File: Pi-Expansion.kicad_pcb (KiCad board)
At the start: 2 copper layers, 66 x 71.1 mm, 17 parts, among them J1 RPi_GPIO, J2 SMA_H, P1 BATT, Q1 IRLML6344TRPBF, U1 A2200-A, U2 SPX2920U-5.0

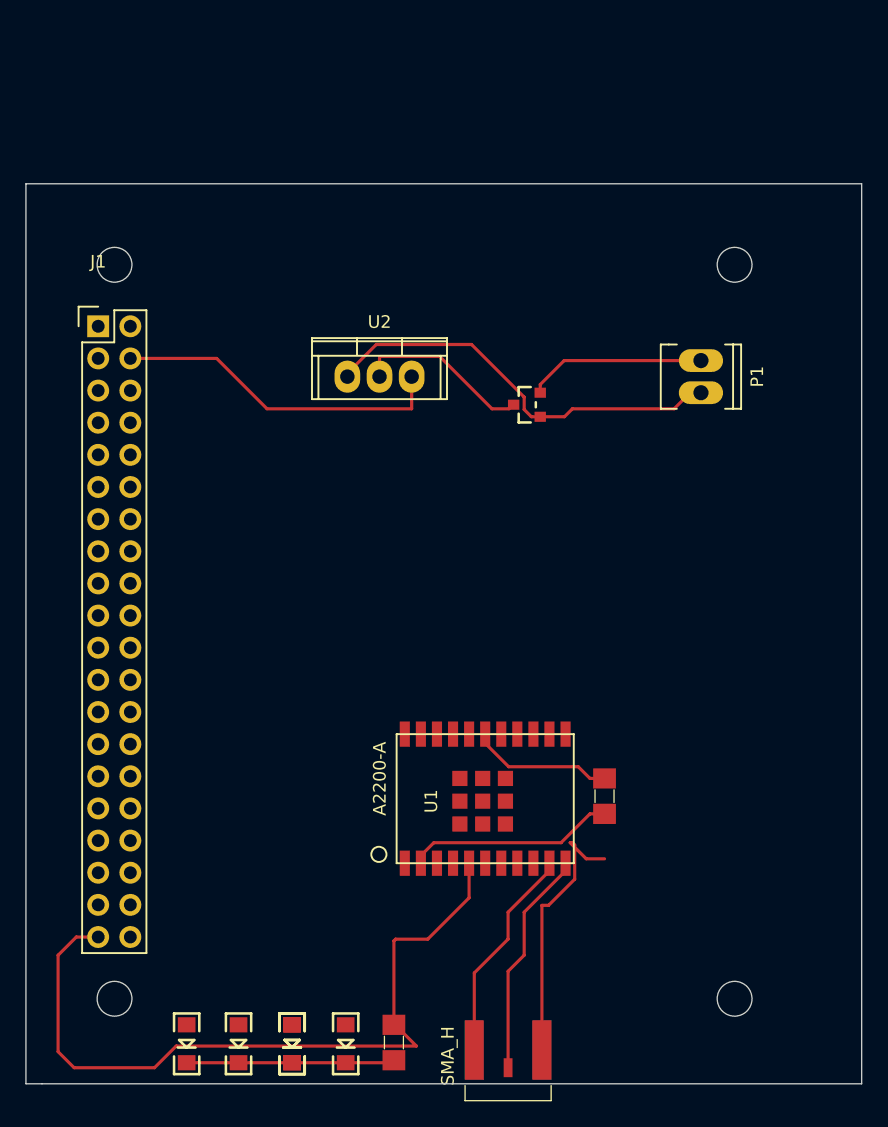
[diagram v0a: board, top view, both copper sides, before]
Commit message: added custom library for arduino board with only mounting holes, also added in the hole position for ardino, and refined pcb outline
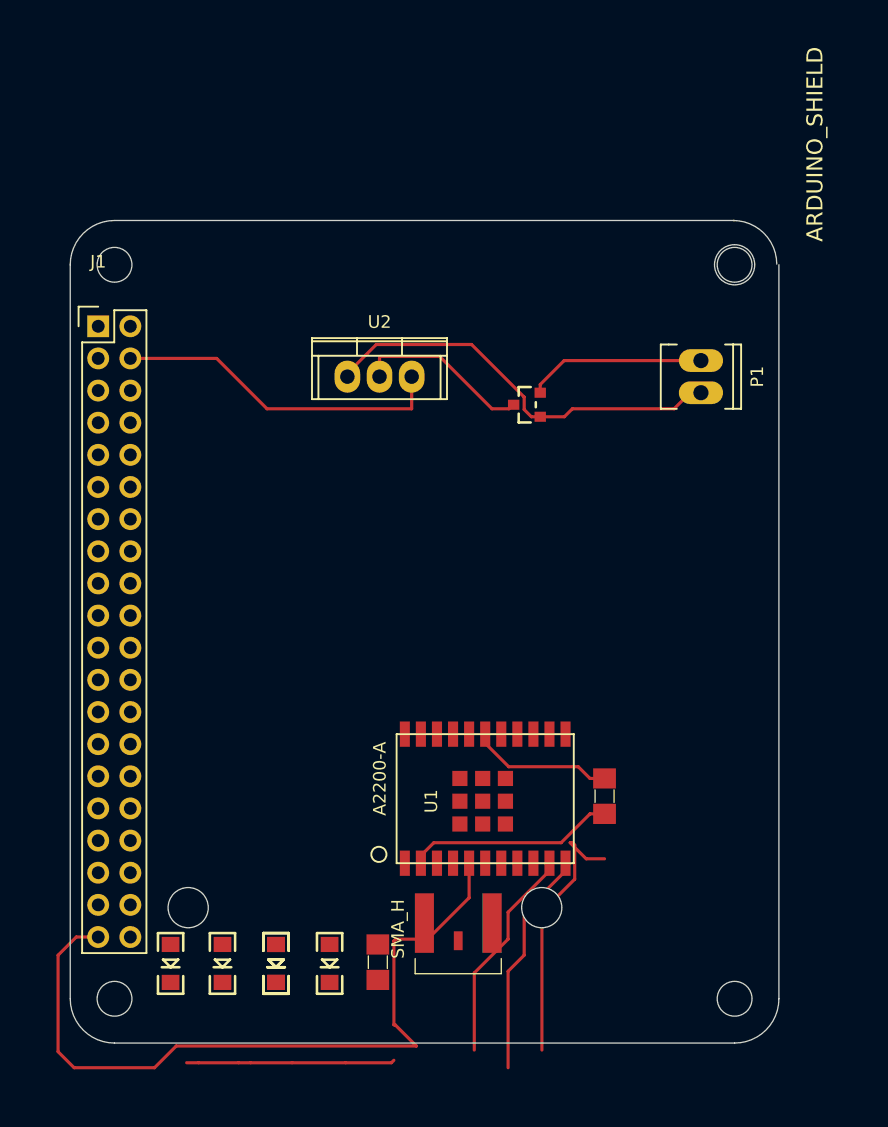
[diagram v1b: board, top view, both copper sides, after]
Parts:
- added ARDUINO_SHIELD: val**, Sailbot_Custom:ARDUINO_SHIELD_3_HOLE, F.Cu at (39.5, 69.9)
- moved J2 10.8 mm to (68.4, 137.2)
- moved R2 6.48 mm to (62.1, 140.2)
- moved LED3 6.48 mm to (49.8, 140.3)
- moved LED4 6.48 mm to (45.7, 140.3)
- moved LED1 6.48 mm to (58.3, 140.3)
- moved LED2 6.48 mm to (54.1, 140.3) (x2)
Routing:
- net (no net): track 0.00 -> 37.7 mm
- net Net-(LED1-PadK): track 16.5 -> 0.00 mm
- net Net-(J2-Pad2): track 38.5 -> 24.6 mm
- net GND: track 74.1 -> 66.8 mm
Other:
- board size 66 x 71.1 mm -> 56 x 65 mm

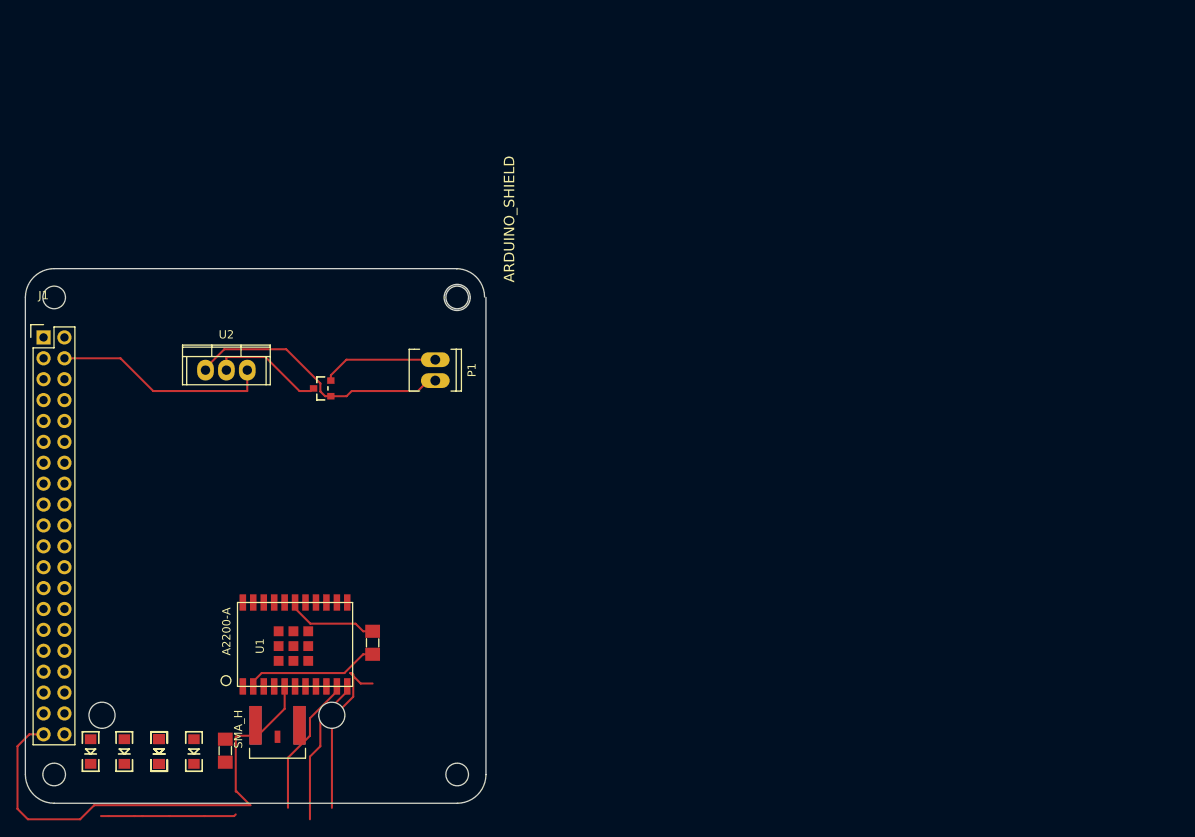
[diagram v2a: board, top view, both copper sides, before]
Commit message: did a full layout of the pcb, should be pretty much compleat, also fixed yet more issues librarys
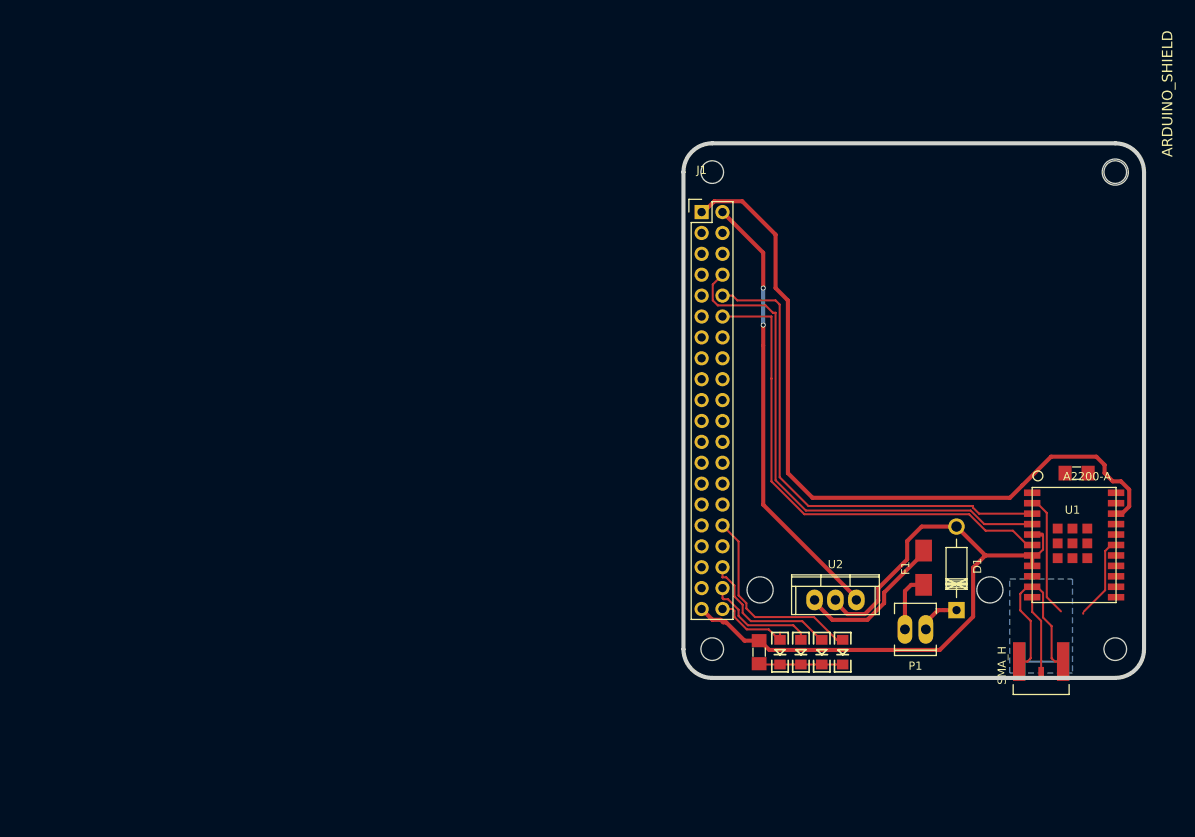
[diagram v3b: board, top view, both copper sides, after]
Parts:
- removed the LED2 at (54.1, 140.3)
- removed Q1: IRLML6344TRPBF, FT:SOT23_FET
- added D1: D, Diodes_ThroughHole:Diode_DO-41_SOD81_Horizontal_RM10, F.Cu at (151.0, 123.2)
- added F1: FUSE, Fuse_Holders_and_Fuses:Fuse_SMD1206_HandSoldering, F.Cu at (147.0, 118.0)
- moved U1 95.5 mm to (165.1, 115.0), turned to 0 degrees
- moved J2 93.2 mm to (161.3, 129.4)
- moved R1 88.0 mm to (165.6, 106.5), turned to 0 degrees
- moved LED4 84.7 mm to (129.5, 128.3)
- moved LED3 83.1 mm to (132.1, 128.3)
- moved LED2 81.5 mm to (134.6, 128.3)
- moved 1121 81.4 mm to (170.3, 127.9)
- moved 1122 81.4 mm to (170.3, 69.9)
- moved J1 81.4 mm to (120.0, 74.8)
- moved 1111 81.4 mm to (121.3, 127.9)
- moved 1112 81.4 mm to (121.3, 69.9)
- moved ARDUINO_SHIELD 81.4 mm to (119.5, 54.7)
- moved LED1 79.8 mm to (137.2, 128.3)
- moved U2 79.1 mm to (136.3, 121.9)
- moved P1 66.3 mm to (146.0, 125.5), turned to 180 degrees
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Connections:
- net GPS_ON_OFF renamed GPS_WAKE
- J1 pad 11: PI_LED_2 -> Net-(J1-Pad11)
- J1 pad 13: PI_LED_3 -> Net-(J1-Pad13)
- J1 pad 15: PI_LED_4 -> Net-(J1-Pad15)
- J1 pad 16: GPS_WAKEUP -> Net-(J1-Pad16)
- J1 pad 18: GPS_RESET -> Net-(J1-Pad18)
- J1 pad 32: Net-(J1-Pad32) -> PI_LED_1
- J1 pad 36: Net-(J1-Pad36) -> PI_LED_2
- J1 pad 38: Net-(J1-Pad38) -> PI_LED_3
- J1 pad 4: +5V -> Net-(J1-Pad4)
- J1 pad 40: Net-(J1-Pad40) -> PI_LED_4
- J1 pad 7: PI_LED_1 -> Net-(J1-Pad7)
- P1 pad 2: Net-(P1-Pad2) -> Net-(F1-Pad1)
- U1 pad 19: GPS_WAKEUP -> GND
- U1 pad 22: GPS_RESET -> Net-(U1-Pad22)
- U2 pad 1: Net-(P1-Pad2) -> Net-(F1-Pad2)
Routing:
- net +3V3: track 0.00 -> 91.9 mm
- net GPS_RX: track 0.00 -> 65.6 mm
- net GPS_TX: track 0.00 -> 61.0 mm
- net GPS_WAKE: track 0.00 -> 60.9 mm
- net (no net): track 37.7 -> 0.53 mm
- net Net-(P1-Pad2): track 32.9 -> 0.00 mm
- net +5V: track 26.4 -> 53.9 mm, vias 0 -> 2
- net PI_LED_1: track 0.00 -> 24.6 mm
- net Net-(F1-Pad2): track 0.00 -> 18.8 mm
- net PI_LED_2: track 0.00 -> 17.8 mm
- net GND: track 67.0 -> 84.1 mm
- net PI_LED_3: track 0.00 -> 13.8 mm
- net Net-(LED1-PadK): track 0.00 -> 10.2 mm
- net PI_LED_4: track 0.00 -> 9.83 mm
- net Net-(D1-Pad1): track 14.1 -> 5.20 mm
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- added copper zone on B.Cu, net Net-(J2-Pad1)
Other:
- outline, holes or cut-outs redrawn
- net class Power added: clearance 0.2, trace_width 0.5, via_dia 0.6, via_drill 0.4

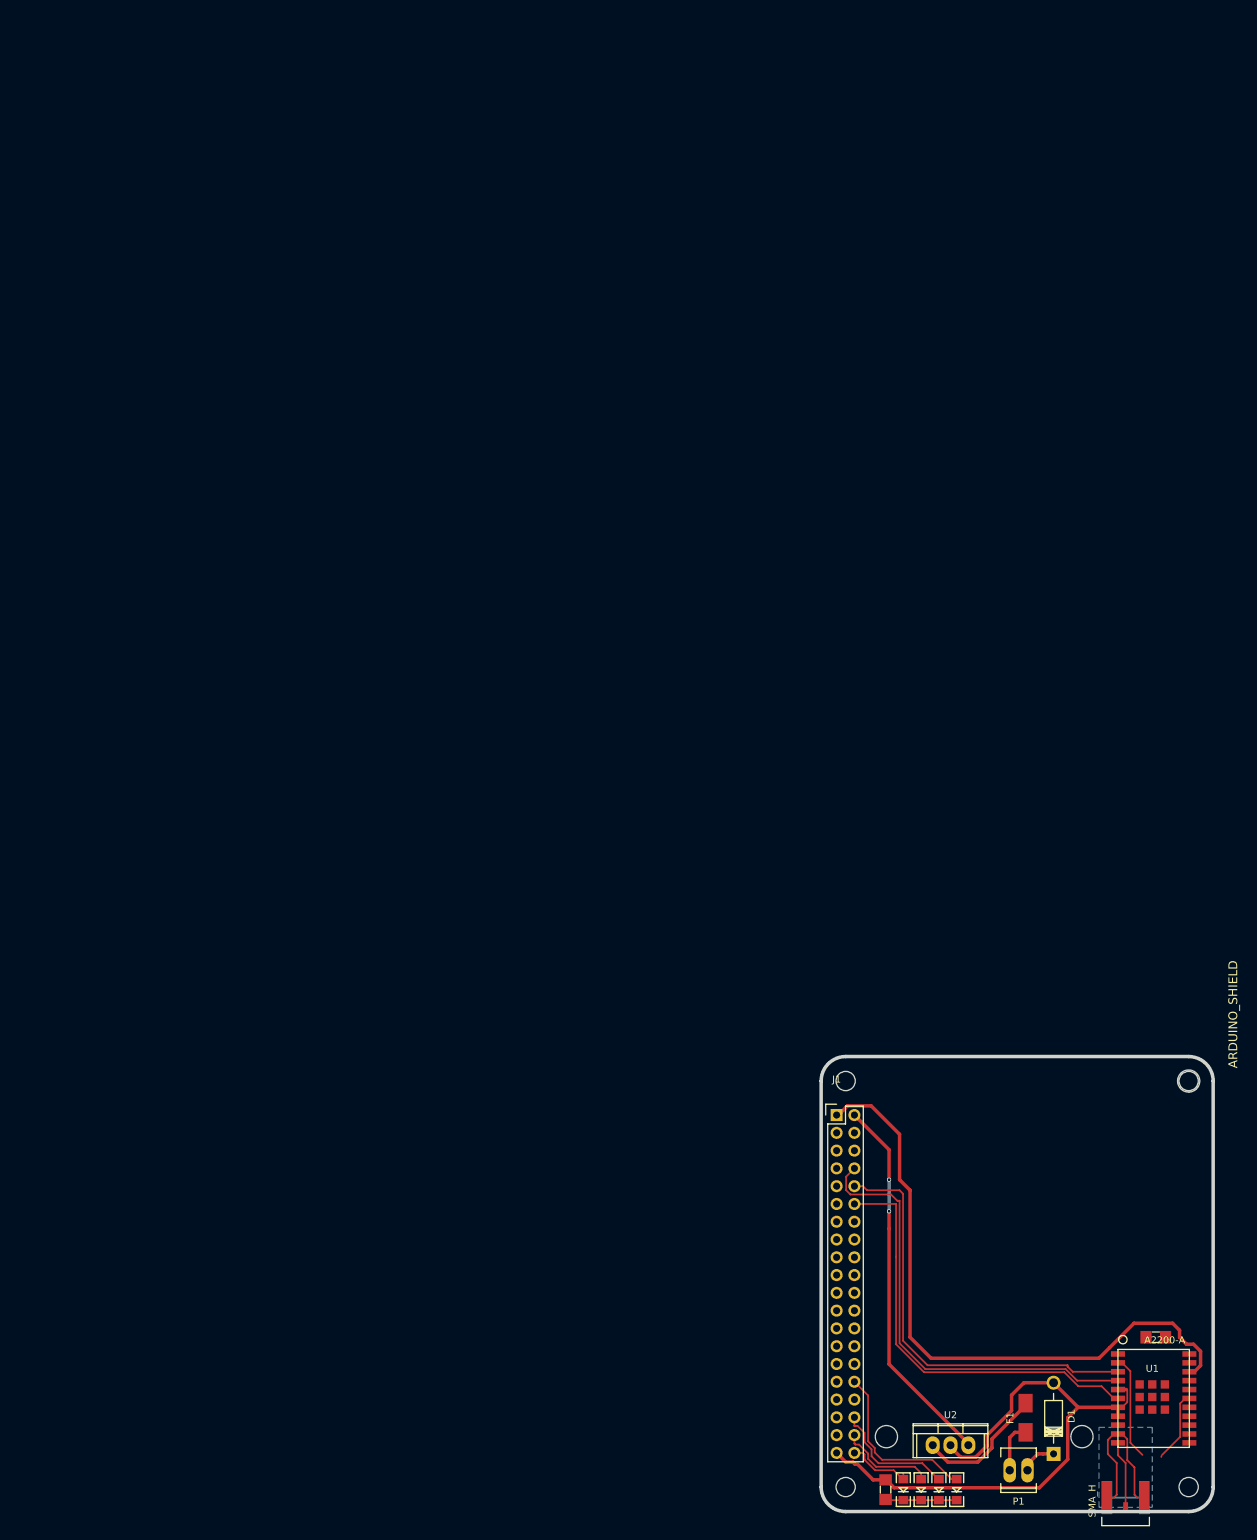
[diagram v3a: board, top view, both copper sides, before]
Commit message: add copper fill for ground plane, and second mill revisions for prototyping
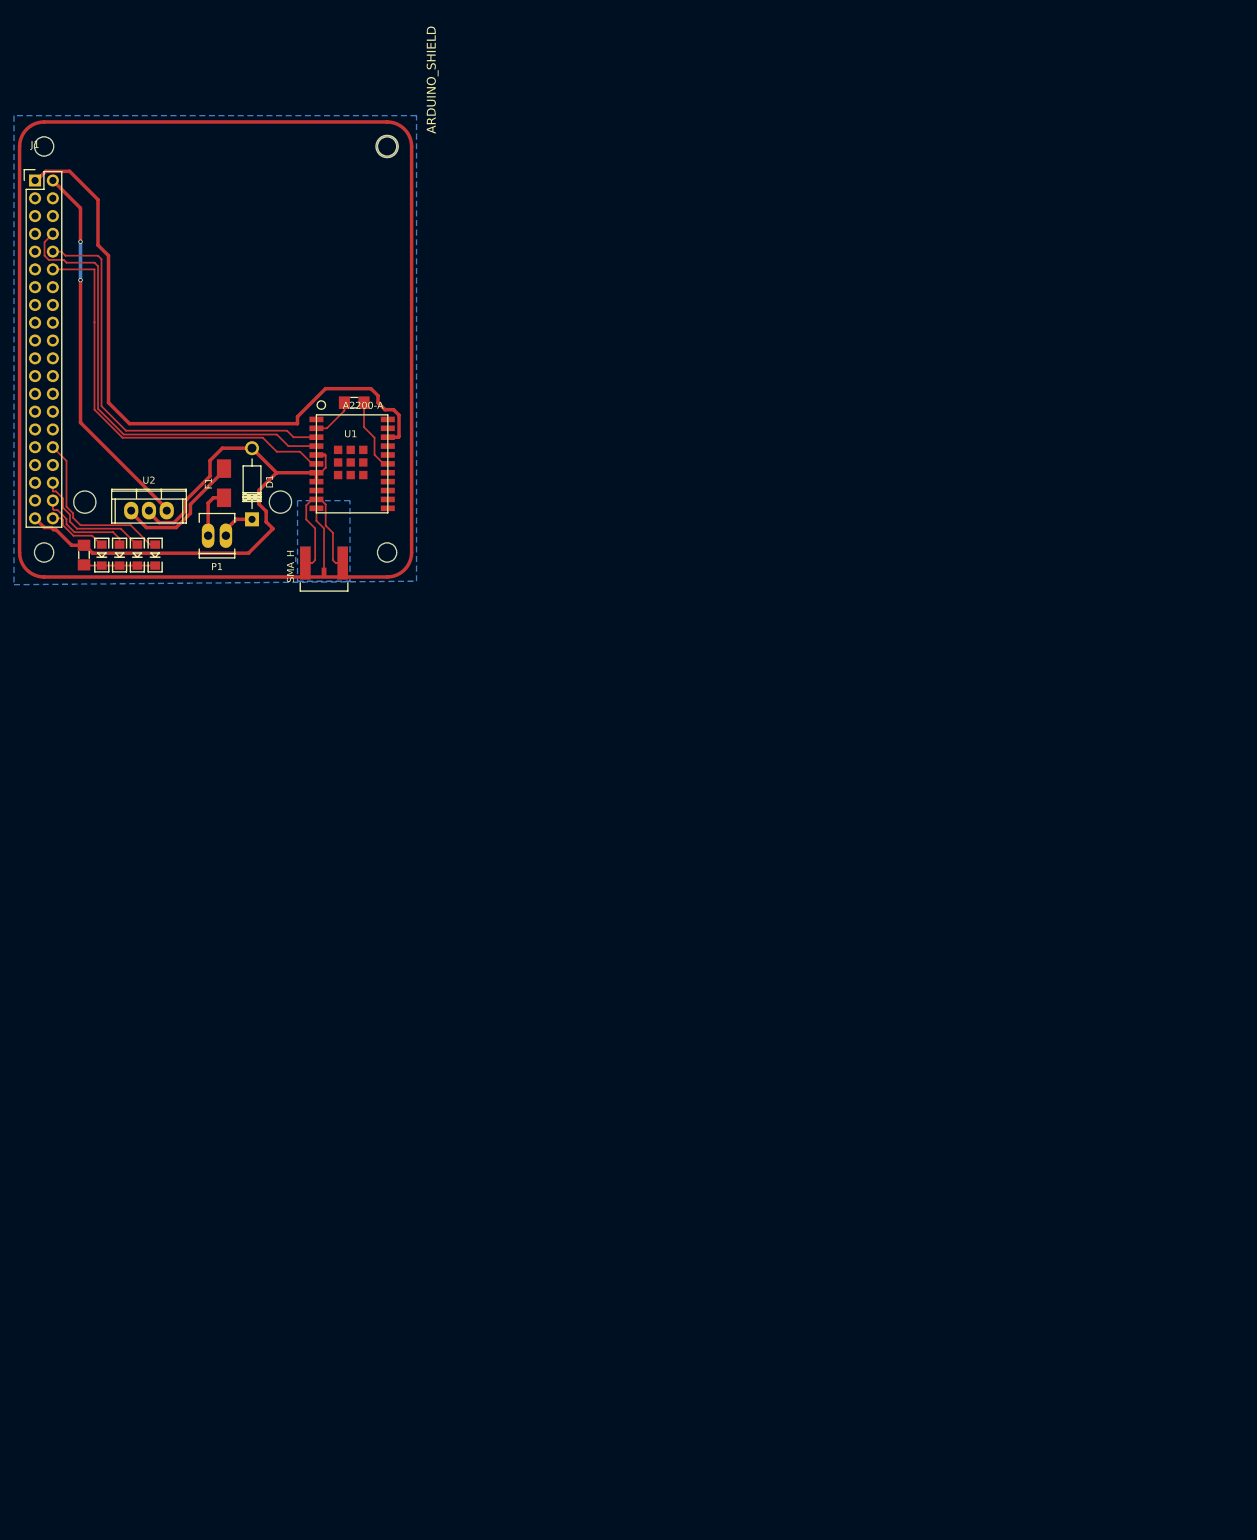
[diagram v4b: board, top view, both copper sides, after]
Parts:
- moved 1111 175.9 mm to (6.80, -5.60)
- moved 1112 175.9 mm to (6.80, -63.6)
- moved 1121 175.9 mm to (55.8, -5.60)
- moved 1122 175.9 mm to (55.8, -63.6)
- moved ARDUINO_SHIELD 175.9 mm to (5.00, -78.8)
- moved D1 175.9 mm to (36.5, -10.3)
- moved F1 175.9 mm to (32.5, -15.5)
- moved J1 175.9 mm to (5.51, -58.7)
- moved J2 175.9 mm to (46.8, -4.09)
- moved LED1 175.9 mm to (22.7, -5.23)
- moved LED2 175.9 mm to (20.1, -5.23)
- moved LED3 175.9 mm to (17.6, -5.23)
- moved LED4 175.9 mm to (15.0, -5.23)
- moved P1 175.9 mm to (31.5, -8.00)
- moved R1 175.9 mm to (51.1, -27.0)
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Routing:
- net Net-(R1-Pad1): track 15.0 -> 6.79 mm
- net Net-(J2-Pad2): track 28.7 -> 23.3 mm
- net GND: track 84.1 -> 86.7 mm
- net +3V3: track 91.9 -> 93.8 mm
- net Net-(F1-Pad1): track 8.51 -> 7.24 mm
- net PI_LED_4: track 9.83 -> 8.98 mm
- added copper zone on B.Cu, net GND
- added copper zone on B.Cu, net Net-(J2-Pad2)
- removed copper zone on B.Cu, net Net-(J2-Pad1)
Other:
- board outline removed
